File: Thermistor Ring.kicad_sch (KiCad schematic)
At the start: 20 parts, among them IC1 MAX30210ENL+, IC2 MAX30210ENL+, IC3 MAX30210ENL+, IC4 MAX30210ENL+, IC5 MAX30210ENL+, IC6 MAX30210ENL+, J1 Conn_01x04_Socket, J3 Conn_01x03_Socket, U1 TPS7A2018PDBVR

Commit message: wip: work on castellated miniboard
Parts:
- added IC7: MAX30210ENL+, MAX30210:21-100600_N90A0&plus_1_ADI, symbol MAX30210:MAX30210ENL+
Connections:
- net INT is gone; now on net GND: IC1.B1 (INT), IC2.B1 (INT), IC3.B1 (INT), IC4.B1 (INT), IC5.B1 (INT), IC6.B1 (INT), J3.2 (Pin_2), R1.2
- net GND: now also IC7.B1 (INT), IC7.B2 (GND_1), IC7.B3 (GND_2)
- net SCL: now also IC7.C2 (SCL)
- net SDA: now also IC7.C1 (SDA)
- net VDD: now also IC7.A1 (VDD)
- new net A0: IC7.A2 (A0)
- new net A1: IC7.A3 (A1)
- new net CVT: IC7.C3 (CVT/PDB)
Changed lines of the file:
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@@
   (junction (at 112.268 36.068) (diameter 0) (color 0 0 0 0)
   )
+  (junction (at 75.438 65.024) (diameter 0) (color 0 0 0 0)
+  )
   (junction (at 119.634 141.224) (diameter 0) (color 0 0 0 0)
   )
@@
   (junction (at 119.634 138.684) (diameter 0) (color 0 0 0 0)
   )
+  (junction (at 75.438 62.484) (diameter 0) (color 0 0 0 0)
+  )
   (junction (at 155.448 69.596) (diameter 0) (color 0 0 0 0)
   )
@@
     (stroke (width 0) (type default))
   )
-  (wire (pts (xy 75.438 59.944) (xy 75.438 69.596))
+  (wire (pts (xy 75.438 59.944) (xy 75.438 62.484))
     (stroke (width 0) (type default))
   )
@@
     (stroke (width 0) (type default))
   )
+  (wire (pts (xy 75.438 62.484) (xy 75.438 65.024))
+    (stroke (width 0) (type default))
+  )
   (wire (pts (xy 166.624 138.176) (xy 168.656 138.176))
     (stroke (width 0) (type default))
@@
     (stroke (width 0) (type default))
   )
+  (wire (pts (xy 75.438 65.024) (xy 75.438 69.596))
+    (stroke (width 0) (type default))
+  )
   (wire (pts (xy 31.496 36.068) (xy 112.268 36.068))
     (stroke (width 0) (type default))
@@
   (label "INT" (at 0 44.958 0) (fields_autoplaced)
     (effects (font (size 1.27 1.27)) (justify left bottom))
+  )
+  (label "VDD" (at 462.28 -19.05 180) (fields_autoplaced)
+    (effects (font (size 1.27 1.27)) (justify right bottom))
+  )
+  (label "SDA" (at 495.3 -16.51 0) (fields_autoplaced)
+    (effects (font (size 1.27 1.27)) (justify left bottom))
+  )
+  (label "CVT" (at 495.3 -11.43 0) (fields_autoplaced)
+    (effects (font (size 1.27 1.27)) (justify left bottom))
+  )
+  (label "A0" (at 462.28 -16.51 180) (fields_autoplaced)
+    (effects (font (size 1.27 1.27)) (justify right bottom))
   )
   (label "CVT{slash}PDB" (at -18.542 69.85 0) (fields_autoplaced)
@@
     (effects (font (size 1.27 1.27)) (justify left bottom))
   )
+  (label "INT" (at 462.28 -11.43 180) (fields_autoplaced)
+    (effects (font (size 1.27 1.27)) (justify right bottom))
+  )
   (label "SDA" (at -19.304 41.148 0) (fields_autoplaced)
     (effects (font (size 1.27 1.27)) (justify left bottom))
   )
+  (label "SCL" (at 495.3 -13.97 0) (fields_autoplaced)
+    (effects (font (size 1.27 1.27)) (justify left bottom))
+  )
   (label "SDA" (at 0 36.068 0) (fields_autoplaced)
     (effects (font (size 1.27 1.27)) (justify left bottom))
@@
     (effects (font (size 1.27 1.27)) (justify left bottom))
   )
+  (label "A1" (at 462.28 -13.97 180) (fields_autoplaced)
+    (effects (font (size 1.27 1.27)) (justify right bottom))
+  )
   (label "ENABLE" (at -18.542 64.77 0) (fields_autoplaced)
     (effects (font (size 1.27 1.27)) (justify left bottom))
   )
   (label "VDD" (at 152.146 -12.192 0) (fields_autoplaced)
+    (effects (font (size 1.27 1.27)) (justify left bottom))
+  )
+  (label "GND" (at 462.28 -8.89 180) (fields_autoplaced)
+    (effects (font (size 1.27 1.27)) (justify right bottom))
+  )
+  (label "GND" (at 495.3 -19.05 0) (fields_autoplaced)
     (effects (font (size 1.27 1.27)) (justify left bottom))
   )
@@
         )
       )
+    )
+  )
+  (symbol (lib_id "MAX30210:MAX30210ENL+") (at 462.28 -19.05 0) (unit 1)
+    (in_bom yes) (on_board yes) (dnp no) (fields_autoplaced)
+    (property "Reference" "IC7" (at 478.79 -26.924 0)
+      (effects (font (size 1.27 1.27)))
+    )
+    (property "Value" "MAX30210ENL+" (at 478.79 -24.384 0)
+      (effects (font (size 1.27 1.27)))
+    )
+    (property "Footprint" "MAX30210:21-100600_N90A0&plus_1_ADI" (at 491.49 -21.59 0)
+      (effects (font (size 1.27 1.27)) (justify left) hide)
+    )
+    (property "Datasheet" "http://www.maximintegrated.com/MAX30210" (at 491.49 -19.05 0)
+      (effects (font (size 1.27 1.27)) (justify left) hide)
+    )
+    (property "Description" "Accurate, Ultra-Small, Low-Power I2C Digital Temperature Sensor" (at 491.49 -16.51 0)
+      (effects (font (size 1.27 1.27)) (justify left) hide)
+    )
+    (property "Height" "0.5" (at 491.49 -13.97 0)
+      (effects (font (size 1.27 1.27)) (justify left) hide)
+    )
+    (property "Mouser Part Number" "" (at 491.49 -11.43 0)
+      (effects (font (size 1.27 1.27)) (justify left) hide)
+    )
+    (property "Mouser Price/Stock" "" (at 491.49 -8.89 0)
+      (effects (font (size 1.27 1.27)) (justify left) hide)
+    )
+    (property "Manufacturer_Name" "Analog Devices" (at 491.49 -6.35 0)
+      (effects (font (size 1.27 1.27)) (justify left) hide)
+    )
+    (property "Manufacturer_Part_Number" "MAX30210ENL+" (at 491.49 -3.81 0)
+      (effects (font (size 1.27 1.27)) (justify left) hide)
+    )
+    (pin "A3")
+    (pin "C1")
+    (pin "B2")
+    (pin "C3")
+    (pin "B1")
+    (pin "A2")
+    (pin "A1")
+    (pin "B3")
+    (pin "C2")
+    (instances
+      (project "Thermistor Ring"
+        (path "/6637e588-6cff-41c7-8818-9eea1dd986d9"
+          (reference "IC7") (unit 1)
+        )
+      )

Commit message: wip: castellated miniboard
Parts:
- removed C1, C2, C3, C4: 0.1uF, Capacitor_SMD:C_0805_2012Metric, symbol Device:C
- removed C5, C6: 0.1uF, Capacitor_SMD:C_0603_1608Metric, symbol Device:C
- removed C7, C8: 1.0uF, Capacitor_SMD:C_0603_1608Metric, symbol Device:C
- removed IC1, IC2, IC3, IC4, IC5, IC6: MAX30210ENL+, MAX30210:21-100600_N90A0&plus_1_ADI, symbol MAX30210:MAX30210ENL+
- removed R1, R2, R3: 4.7k, Resistor_SMD:R_0805_2012Metric, symbol Device:R
- removed U1: TPS7A2018PDBVR, TPS7A201:DBV0005A-IPC_A, symbol TI_LDO_ TPS7A2018PDBVR:TPS7A2018PDBVR
- added C9: 0.1uF, Capacitor_SMD:C_0805_2012Metric, symbol Device:C
- IC7: footprint MAX30210:21-100600_N90A0&plus_1_ADI -> MAX30210ENL:21-100600_N90A0&plus_1_ADI
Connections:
- net GND: now also C9.2; no longer IC7.B1 (INT), J3.2 (Pin_2)
- net VDD: now also C9.1
- new net INT: IC7.B1 (INT), J3.2 (Pin_2)
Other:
- moved on the sheet: IC7, J1

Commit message: layout for manufacturing
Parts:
- removed J3: Conn_01x03_Socket, Connector_JST:JST_XH_B3B-XH-A_1x03_P2.50mm_Vertical, symbol Connector:Conn_01x03_Socket
- added J2: Conn_01x04_Socket, Connector_PinSocket_2.00mm:PinSocket_1x04_P2.00mm_Vertical, symbol Connector:Conn_01x04_Socket
- added U1: ~, Temp_Sensor_Breakout:Temp_Sensor_Breakout_1.0, symbol TempSensorBreakout:TempSensorBreakout
- J1: footprint Connector_JST:JST_XH_B4B-XH-A_1x04_P2.50mm_Vertical -> Connector_PinSocket_2.00mm:PinSocket_1x04_P2.00mm_Vertical
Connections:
- net Power 3.3-5V is gone; now on net A0: J1.2 (Pin_2)
- net A0: now also U1.2 (A0)
- net A1: now also J1.1 (Pin_1), U1.1 (A1)
- net CVT: now also J2.1 (Pin_1), U1.5 (CVT)
- net GND: now also J2.4 (Pin_4), U1.8 (GND); no longer J1.1 (Pin_1)
- net INT: now also J1.3 (Pin_3), U1.3 (INT)
- net SCL: now also J2.2 (Pin_2), U1.6 (SCL); no longer J1.4 (Pin_4)
- net SDA: now also J2.3 (Pin_3), U1.7 (SDA); no longer J1.3 (Pin_3)
- net VDD: now also J1.4 (Pin_4), U1.4 (VDD)
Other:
- moved on the sheet: J1
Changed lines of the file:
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@@
 (kicad_sch (version 20230121) (generator eeschema)
   (paper "A4")
+  (wire (pts (xy 175.26 50.8) (xy 187.96 50.8))
+    (stroke (width 0) (type default))
+  )
   (wire (pts (xy 69.85 44.45) (xy 83.82 44.45))
     (stroke (width 0) (type default))
   )
+  (wire (pts (xy 175.26 45.72) (xy 187.96 45.72))
+    (stroke (width 0) (type default))
+  )
+  (wire (pts (xy 175.26 48.26) (xy 187.96 48.26))
+    (stroke (width 0) (type default))
+  )
+  (wire (pts (xy 149.86 50.8) (xy 160.02 50.8))
+    (stroke (width 0) (type default))
+  )
   (wire (pts (xy 69.85 52.07) (xy 69.85 52.832))
     (stroke (width 0) (type default))
   )
-  (label "INT" (at 33.782 74.422 0) (fields_autoplaced)
-    (effects (font (size 1.27 1.27)) (justify left bottom))
+  (wire (pts (xy 149.86 43.18) (xy 160.02 43.18))
+    (stroke (width 0) (type default))
+  )
+  (wire (pts (xy 149.86 48.26) (xy 160.02 48.26))
+    (stroke (width 0) (type default))
+  )
+  (wire (pts (xy 149.86 45.72) (xy 160.02 45.72))
+    (stroke (width 0) (type default))
+  )
+  (wire (pts (xy 175.26 43.18) (xy 187.96 43.18))
+    (stroke (width 0) (type default))
   )
   (label "VDD" (at 83.82 44.45 180) (fields_autoplaced)
@@
     (effects (font (size 1.27 1.27)) (justify right bottom))
   )
-  (label "CVT{slash}PDB" (at 33.782 76.962 0) (fields_autoplaced)
-    (effects (font (size 1.27 1.27)) (justify left bottom))
-  )
-  (label "Power 3.3-5V" (at 33.02 50.8 0) (fields_autoplaced)
+  (label "CVT" (at 181.61 43.18 0) (fields_autoplaced)
+    (effects (font (size 1.27 1.27)) (justify left bottom))
+  )
+  (label "A1" (at 153.67 43.18 0) (fields_autoplaced)
+    (effects (font (size 1.27 1.27)) (justify left bottom))
+  )
+  (label "VDD" (at 153.67 50.8 0) (fields_autoplaced)
     (effects (font (size 1.27 1.27)) (justify left bottom))
   )
@@
     (effects (font (size 1.27 1.27)) (justify right bottom))
   )
-  (label "SDA" (at 33.02 48.26 0) (fields_autoplaced)
+  (label "SDA" (at 181.61 48.26 0) (fields_autoplaced)
     (effects (font (size 1.27 1.27)) (justify left bottom))
   )
@@
     (effects (font (size 1.27 1.27)) (justify left bottom))
   )
-  (label "SCL" (at 33.02 45.72 0) (fields_autoplaced)
+  (label "INT" (at 153.67 48.26 0) (fields_autoplaced)
     (effects (font (size 1.27 1.27)) (justify left bottom))
   )
@@
     (effects (font (size 1.27 1.27)) (justify right bottom))
   )
-  (label "ENABLE" (at 33.782 71.882 0) (fields_autoplaced)
+  (label "SCL" (at 181.61 45.72 0) (fields_autoplaced)
     (effects (font (size 1.27 1.27)) (justify left bottom))
   )
@@
     (effects (font (size 1.27 1.27)) (justify left bottom))
   )
-  (label "GND" (at 33.02 53.34 0) (fields_autoplaced)
-    (effects (font (size 1.27 1.27)) (justify left bottom))
-  )
-  (symbol (lib_id "Connector:Conn_01x04_Socket") (at 27.94 50.8 180) (unit 1)
-    (in_bom yes) (on_board yes) (dnp no) (fields_autoplaced)
-    (property "Reference" "J1" (at 28.575 40.132 0)
-      (effects (font (size 1.27 1.27)))
-    )
-    (property "Value" "Conn_01x04_Socket" (at 28.575 42.672 0)
-      (effects (font (size 1.27 1.27)))
-    )
-    (property "Footprint" "Connector_JST:JST_XH_B4B-XH-A_1x04_P2.50mm_Vertical" (at 27.94 50.8 0)
-      (effects (font (size 1.27 1.27)) hide)
-    )
-    (property "Datasheet" "~" (at 27.94 50.8 0)
+  (label "GND" (at 181.61 50.8 0) (fields_autoplaced)
+    (effects (font (size 1.27 1.27)) (justify left bottom))
+  )
+  (label "A0" (at 153.67 45.72 0) (fields_autoplaced)
+    (effects (font (size 1.27 1.27)) (justify left bottom))
+  )
+  (symbol (lib_id "Connector:Conn_01x04_Socket") (at 144.78 45.72 0) (mirror y) (unit 1)
+    (in_bom yes) (on_board yes) (dnp no)
+    (property "Reference" "J1" (at 145.415 55.88 0)
+      (effects (font (size 1.27 1.27)))
+    )
+    (property "Value" "Conn_01x04_Socket" (at 145.415 53.34 0)
+      (effects (font (size 1.27 1.27)))
+    )
+    (property "Footprint" "Connector_PinSocket_2.00mm:PinSocket_1x04_P2.00mm_Vertical" (at 144.78 45.72 0)
+      (effects (font (size 1.27 1.27)) hide)
+    )
+    (property "Datasheet" "~" (at 144.78 45.72 0)
       (effects (font (size 1.27 1.27)) hide)
     )
@@
     )
   )
+  (symbol (lib_id "TempSensorBreakout:TempSensorBreakout") (at 167.64 45.72 0) (unit 1)
+    (in_bom yes) (on_board yes) (dnp no) (fields_autoplaced)
+    (property "Reference" "U1" (at 167.64 39.37 0)
+      (effects (font (size 1.27 1.27)))
+    )
+    (property "Value" "~" (at 167.64 45.72 0)
+      (effects (font (size 1.27 1.27)))
+    )
+    (property "Footprint" "Temp_Sensor_Breakout:Temp_Sensor_Breakout_1.0" (at 167.64 45.72 0)
+      (effects (font (size 1.27 1.27)) hide)
+    )
+    (property "Datasheet" "" (at 167.64 45.72 0)
+      (effects (font (size 1.27 1.27)) hide)
+    )
+    (pin "6")
+    (pin "7")
+    (pin "4")
+    (pin "3")
+    (pin "1")
+    (pin "2")
+    (pin "8")
+    (pin "5")
+    (instances
+      (project "Thermistor Ring"
+        (path "/6637e588-6cff-41c7-8818-9eea1dd986d9"
+          (reference "U1") (unit 1)
+        )
+      )
+    )
+  )
   (symbol (lib_id "Device:C") (at 69.85 48.26 0) (unit 1)
     (in_bom yes) (on_board yes) (dnp no) (fields_autoplaced)
@@
     )
   )
-  (symbol (lib_id "Connector:Conn_01x03_Socket") (at 28.702 74.422 180) (unit 1)
-    (in_bom yes) (on_board yes) (dnp no) (fields_autoplaced)
-    (property "Reference" "J3" (at 29.337 66.04 0)
-      (effects (font (size 1.27 1.27)) hide)
-    )
-    (property "Value" "Conn_01x03_Socket" (at 29.337 69.342 0)
-      (effects (font (size 1.27 1.27)))
-    )
-    (property "Footprint" "Connector_JST:JST_XH_B3B-XH-A_1x03_P2.50mm_Vertical" (at 28.702 74.422 0)
-      (effects (font (size 1.27 1.27)) hide)
-    )
-    (property "Datasheet" "~" (at 28.702 74.422 0)
-      (effects (font (size 1.27 1.27)) hide)
-    )
-    (pin "2")
+  (symbol (lib_id "power:GND") (at 69.85 52.832 0) (unit 1)
+    (in_bom yes) (on_board yes) (dnp no) (fields_autoplaced)
+    (property "Reference" "#PWR017" (at 69.85 59.182 0)
+      (effects (font (size 1.27 1.27)) hide)
+    )
+    (property "Value" "GND" (at 69.85 58.166 0)
+      (effects (font (size 1.27 1.27)))
+    )
+    (property "Footprint" "" (at 69.85 52.832 0)
+      (effects (font (size 1.27 1.27)) hide)
+    )
+    (property "Datasheet" "" (at 69.85 52.832 0)
+      (effects (font (size 1.27 1.27)) hide)
+    )
+    (pin "1")
+    (instances
+      (project "Thermistor Ring"
+        (path "/6637e588-6cff-41c7-8818-9eea1dd986d9"
+          (reference "#PWR017") (unit 1)
+        )
+      )
+    )
+  )
+  (symbol (lib_id "Connector:Conn_01x04_Socket") (at 193.04 45.72 0) (unit 1)
+    (in_bom yes) (on_board yes) (dnp no) (fields_autoplaced)
+    (property "Reference" "J2" (at 194.31 45.72 0)
+      (effects (font (size 1.27 1.27)) (justify left))
+    )
+    (property "Value" "Conn_01x04_Socket" (at 194.31 48.26 0)
+      (effects (font (size 1.27 1.27)) (justify left))
+    )
+    (property "Footprint" "Connector_PinSocket_2.00mm:PinSocket_1x04_P2.00mm_Vertical" (at 193.04 45.72 0)
+      (effects (font (size 1.27 1.27)) hide)
+    )
+    (property "Datasheet" "~" (at 193.04 45.72 0)
+      (effects (font (size 1.27 1.27)) hide)
+    )
+    (pin "1")
+    (pin "4")
     (pin "3")
-    (pin "1")
-    (instances
-      (project "Thermistor Ring"
-        (path "/6637e588-6cff-41c7-8818-9eea1dd986d9"
-          (reference "J3") (unit 1)
-        )
-      )
-    )
-  )
-  (symbol (lib_id "power:GND") (at 69.85 52.832 0) (unit 1)
-    (in_bom yes) (on_board yes) (dnp no) (fields_autoplaced)
-    (property "Reference" "#PWR017" (at 69.85 59.182 0)
-      (effects (font (size 1.27 1.27)) hide)
-    )
-    (property "Value" "GND" (at 69.85 58.166 0)
-      (effects (font (size 1.27 1.27)))
-    )
-    (property "Footprint" "" (at 69.85 52.832 0)
-      (effects (font (size 1.27 1.27)) hide)
-    )
-    (property "Datasheet" "" (at 69.85 52.832 0)
-      (effects (font (size 1.27 1.27)) hide)
-    )
-    (pin "1")
-    (instances
-      (project "Thermistor Ring"
-        (path "/6637e588-6cff-41c7-8818-9eea1dd986d9"
-          (reference "#PWR017") (unit 1)
-        )
-      )
+    (pin "2")
+    (instances
+      (project "Thermistor Ring"
+        (path "/6637e588-6cff-41c7-8818-9eea1dd986d9"
+          (reference "J2") (unit 1)
+        )
+      )

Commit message: wip: flawed initial array layout attempt
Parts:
- C1: renamed from C9; footprint Capacitor_SMD:C_0805_2012Metric -> Capacitor_SMD:C_0603_1608Metric
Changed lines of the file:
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@@
   (symbol (lib_id "Device:C") (at 69.85 48.26 0) (unit 1)
     (in_bom yes) (on_board yes) (dnp no) (fields_autoplaced)
-    (property "Reference" "C9" (at 73.66 46.99 0)
+    (property "Reference" "C1" (at 73.66 46.99 0)
       (effects (font (size 1.27 1.27)) (justify left))
     )
@@
       (effects (font (size 1.27 1.27)) (justify left))
     )
-    (property "Footprint" "Capacitor_SMD:C_0805_2012Metric" (at 70.8152 52.07 0)
+    (property "Footprint" "Capacitor_SMD:C_0603_1608Metric" (at 70.8152 52.07 0)
       (effects (font (size 1.27 1.27)) hide)
     )
@@
       (project "Thermistor Ring"
         (path "/6637e588-6cff-41c7-8818-9eea1dd986d9"
-          (reference "C9") (unit 1)
+          (reference "C1") (unit 1)
         )
       )

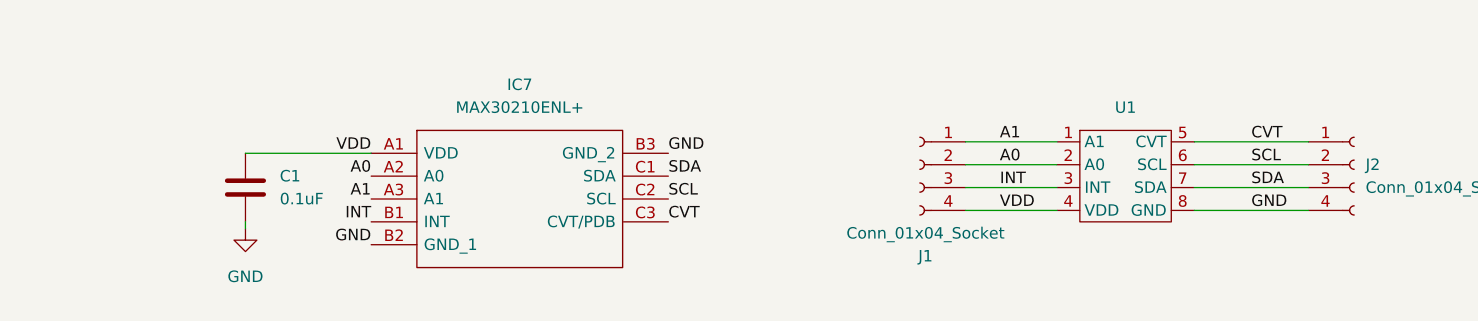
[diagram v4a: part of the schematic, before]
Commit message: castellated temp board, updated footprint, array layout
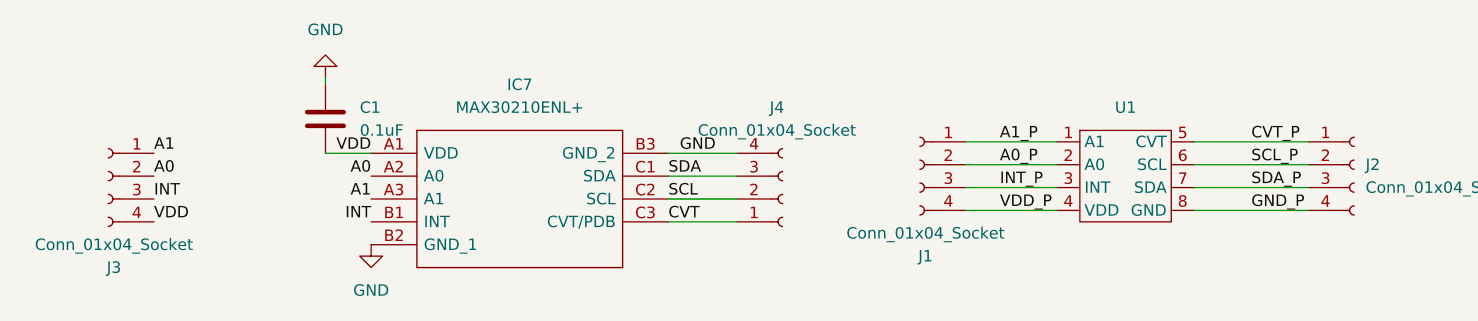
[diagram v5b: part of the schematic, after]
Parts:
- added J3, J4: Conn_01x04_Socket, Connector_PinSocket_1.27mm:PinSocket_1x04_P1.27mm_Vertical, symbol Connector:Conn_01x04_Socket
- C1: footprint Capacitor_SMD:C_0603_1608Metric -> Capacitor_SMD:C_0402_1005Metric; Manufacturer_Name (none) -> Samsung Electro-Mechanics; Manufacturer_Part_Number (none) -> CL05A104KA5NNNC
- J1, J2, U1: DNI (none) -> DNI
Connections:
- net A0: now also J3.2 (Pin_2); no longer J1.2 (Pin_2), U1.2 (A0)
- net A1: now also J3.1 (Pin_1); no longer J1.1 (Pin_1), U1.1 (A1)
- net CVT: now also J4.1 (Pin_1); no longer J2.1 (Pin_1), U1.5 (CVT)
- net GND: now also J4.4 (Pin_4); no longer J2.4 (Pin_4), U1.8 (GND)
- net INT: now also J3.3 (Pin_3); no longer J1.3 (Pin_3), U1.3 (INT)
- net SCL: now also J4.2 (Pin_2); no longer J2.2 (Pin_2), U1.6 (SCL)
- net SDA: now also J4.3 (Pin_3); no longer J2.3 (Pin_3), U1.7 (SDA)
- net VDD: now also J3.4 (Pin_4); no longer J1.4 (Pin_4), U1.4 (VDD)
- new net A0_P: J1.2 (Pin_2), U1.2 (A0)
- new net A1_P: J1.1 (Pin_1), U1.1 (A1)
- new net CVT_P: J2.1 (Pin_1), U1.5 (CVT)
- new net GND_P: J2.4 (Pin_4), U1.8 (GND)
- new net INT_P: J1.3 (Pin_3), U1.3 (INT)
- new net SCL_P: J2.2 (Pin_2), U1.6 (SCL)
- new net SDA_P: J2.3 (Pin_3), U1.7 (SDA)
- new net VDD_P: J1.4 (Pin_4), U1.4 (VDD)
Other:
- moved on the sheet: C1
